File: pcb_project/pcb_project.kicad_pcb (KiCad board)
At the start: 8 copper layers, 234 parts, among them IC1 TPS54325PWPR, IC2 TPS54294PWPR, IC3 IS61WV204816BLL-10TLI, J1 Conn_01x10_Pin, J2 FTSH-107-01-F-DV-K, J3 Conn_ST_STDC14, J4 DE15_Socket_HighDensity_Mount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, J5 USB_B_Micro, J6 MEM2052-00-195-00-A, J7 USB_A, Q1 BC857BS, Q2 BC847BPN, U1 XC7A100T-FTG256, U2 STM32U595VJTx, U3 TPS2041B, U4 D3V3XA4B10LP, U7 MAX7221xWG, U8 COM-11405, U9 MT25QL128ABA1ESE-0SIT, Y1 48MHz, Y2 XLH736025.175000I

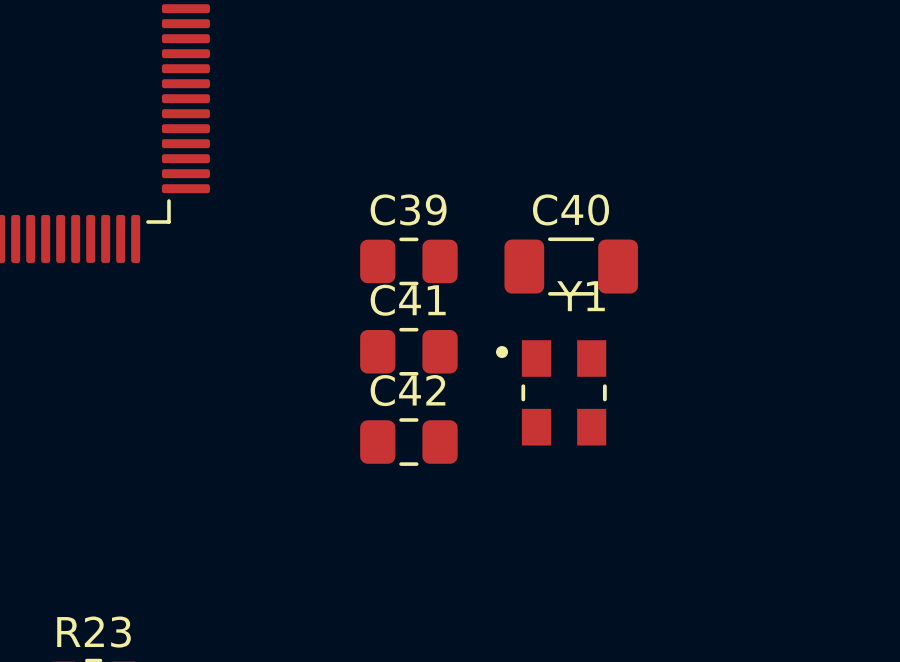
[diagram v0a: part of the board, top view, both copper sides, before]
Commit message: Add debounce cap on FPGA reset, add second sram symbol
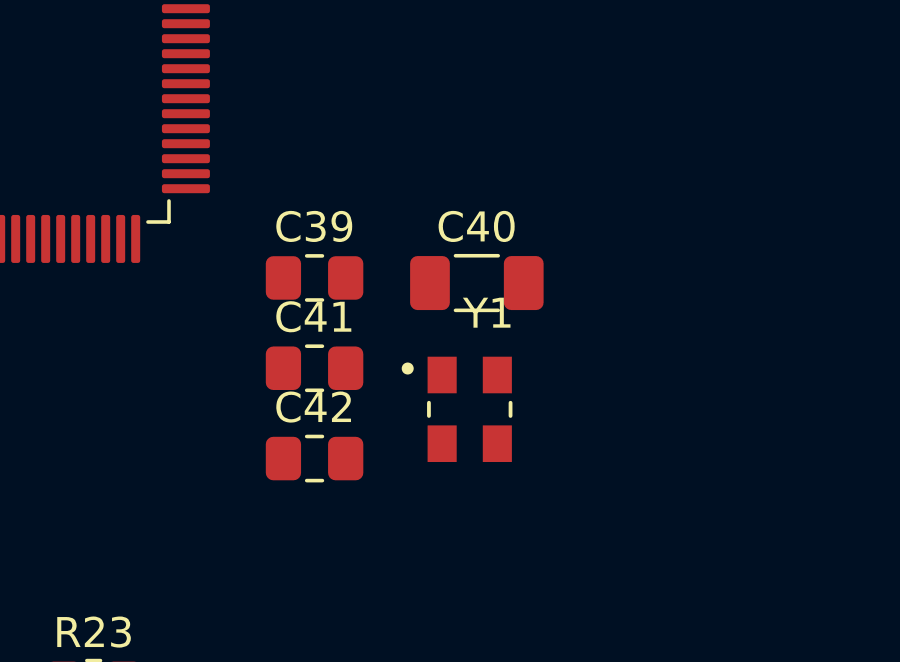
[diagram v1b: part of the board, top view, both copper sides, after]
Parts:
- moved C41 3.19 mm to (205.0, 124.5)
- moved C39 3.19 mm to (205.0, 121.5)
- moved C40 3.19 mm to (210.4, 121.7)
- moved C42 3.19 mm to (205.0, 127.5)
- moved Y1 3.19 mm to (210.1, 125.9)
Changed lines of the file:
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@@
 	(footprint "Capacitor_SMD:C_0805_2012Metric_Pad1.18x1.45mm_HandSolder"
 		(layer "F.Cu")
-		(at 208.107 126.97)
+		(at 204.9625 127.52)
 		(descr "Capacitor SMD 0805 (2012 Metric), square (rectangular) end terminal, IPC-7351 nominal with elongated pad for handsoldering. (Body size source: IPC-SM-782 page 76, https://www.pcb-3d.com/wordpress/wp-content/uploads/ipc-sm-782a_amendment_1_and_2.pdf, https://docs.google.com/spreadsheets/d/1BsfQQcO9C6DZCsRaXUlFlo91Tg2WpOkGARC1WS5S8t0/edit?usp=sharing), generated with kicad-footprint-generator")
 		(tags "capacitor handsolder")
@@
 	(footprint "Project_Footprints:OSCCC320X250X60N"
 		(layer "F.Cu")
-		(at 213.28 125.33)
+		(at 210.1355 125.88)
 		(property "Reference" "Y1"
 			(at 0.62907 -3.18457 0)
@@
 	(footprint "Capacitor_SMD:C_0805_2012Metric_Pad1.18x1.45mm_HandSolder"
 		(layer "F.Cu")
-		(at 208.107 123.96)
+		(at 204.9625 124.51)
 		(descr "Capacitor SMD 0805 (2012 Metric), square (rectangular) end terminal, IPC-7351 nominal with elongated pad for handsoldering. (Body size source: IPC-SM-782 page 76, https://www.pcb-3d.com/wordpress/wp-content/uploads/ipc-sm-782a_amendment_1_and_2.pdf, https://docs.google.com/spreadsheets/d/1BsfQQcO9C6DZCsRaXUlFlo91Tg2WpOkGARC1WS5S8t0/edit?usp=sharing), generated with kicad-footprint-generator")
 		(tags "capacitor handsolder")
@@
 	(footprint "Capacitor_SMD:C_1206_3216Metric_Pad1.33x1.80mm_HandSolder"
 		(layer "F.Cu")
-		(at 213.517 121.12)
+		(at 210.3725 121.67)
 		(descr "Capacitor SMD 1206 (3216 Metric), square (rectangular) end terminal, IPC-7351 nominal with elongated pad for handsoldering. (Body size source: IPC-SM-782 page 76, https://www.pcb-3d.com/wordpress/wp-content/uploads/ipc-sm-782a_amendment_1_and_2.pdf), generated with kicad-footprint-generator")
 		(tags "capacitor handsolder")
@@
 	(footprint "Capacitor_SMD:C_0805_2012Metric_Pad1.18x1.45mm_HandSolder"
 		(layer "F.Cu")
-		(at 208.107 120.95)
+		(at 204.9625 121.5)
 		(descr "Capacitor SMD 0805 (2012 Metric), square (rectangular) end terminal, IPC-7351 nominal with elongated pad for handsoldering. (Body size source: IPC-SM-782 page 76, https://www.pcb-3d.com/wordpress/wp-content/uploads/ipc-sm-782a_amendment_1_and_2.pdf, https://docs.google.com/spreadsheets/d/1BsfQQcO9C6DZCsRaXUlFlo91Tg2WpOkGARC1WS5S8t0/edit?usp=sharing), generated with kicad-footprint-generator")
 		(tags "capacitor handsolder")

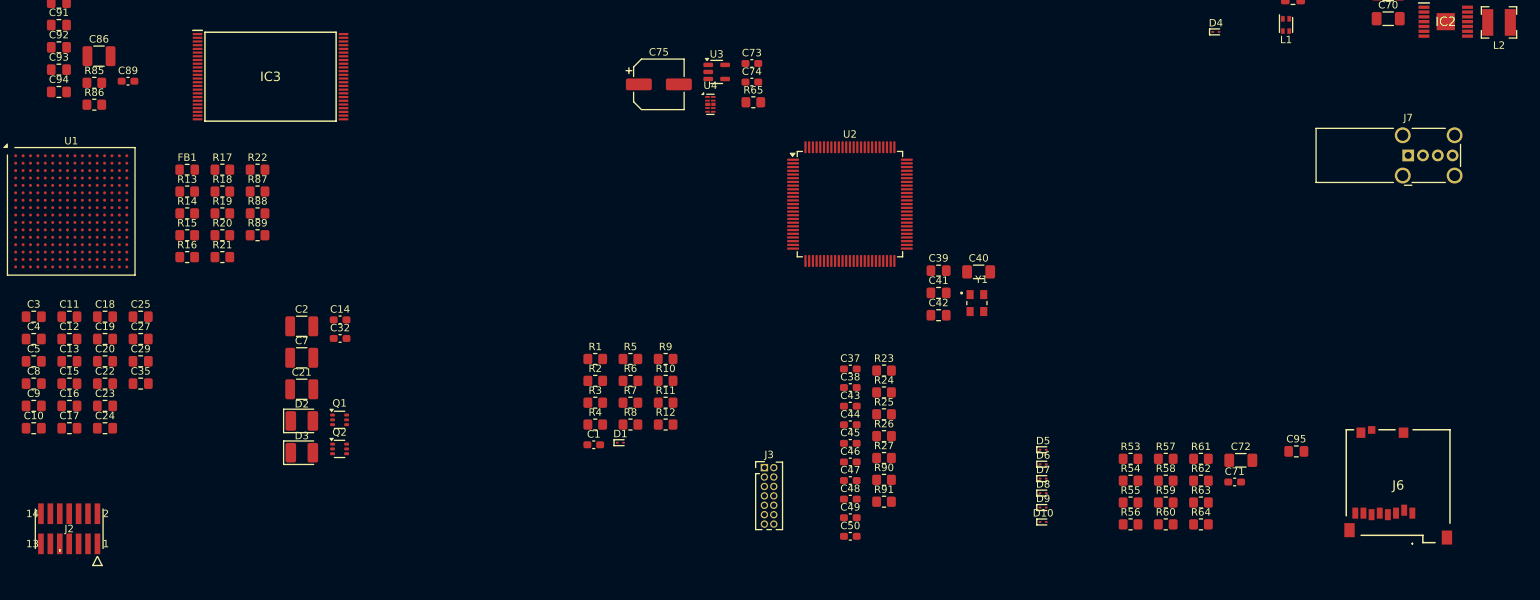
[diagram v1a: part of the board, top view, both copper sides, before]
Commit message: Initial MicroSD reader layout
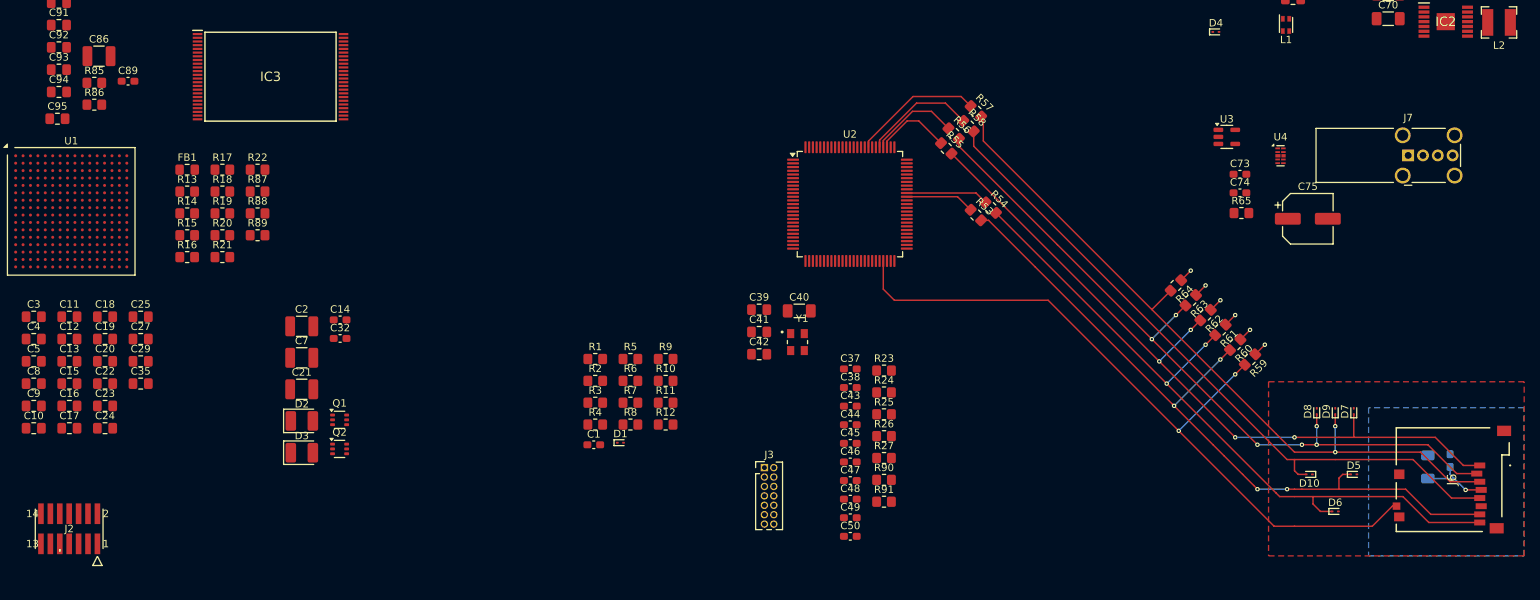
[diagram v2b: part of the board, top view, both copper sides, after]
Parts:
- C71, C72: moved to B.Cu
- moved C95 173.1 mm to (86.0, 101.0)
- moved C75 89.4 mm to (254.8, 114.5)
- moved U4 77.3 mm to (251.1, 106.0)
- moved U3 69.4 mm to (243.9, 103.5)
- moved C73 67.6 mm to (245.6, 108.5)
- moved C74 67.6 mm to (245.6, 111.0)
- moved R65 67.6 mm to (245.8, 113.7)
- moved R56 57.9 mm to (207.0, 103.0), turned to -45 degrees
- moved R58 54.8 mm to (209.0, 102.0), turned to -45 degrees
- moved R55 53.9 mm to (206.0, 105.0), turned to -45 degrees
- moved R57 53.4 mm to (210.0, 100.0), turned to -45 degrees
- moved D7 42.9 mm to (261.0, 140.5), turned to 90 degrees
- moved D5 42.1 mm to (261.0, 149.0)
- moved D9 41.5 mm to (258.5, 140.5), turned to 90 degrees
- moved R54 41.4 mm to (212.0, 113.0), turned to -45 degrees
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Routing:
- net /MCU/PB10_LPGPIO1_P4: track 0.00 -> 100.1 mm, vias 0 -> 2
- net Net-(D8-A1): track 0.00 -> 99.7 mm, vias 0 -> 6
- net Net-(D7-A1): track 0.00 -> 99.6 mm, vias 0 -> 4
- net Net-(D9-A1): track 0.00 -> 98.1 mm, vias 0 -> 2
- net Net-(D5-A1): track 0.00 -> 97.7 mm, vias 0 -> 4
- net Net-(D6-A1): track 0.00 -> 96.5 mm, vias 0 -> 2
- net Net-(D10-A2): track 0.00 -> 93.3 mm
- net +3V3: track 0.00 -> 20.6 mm, vias 0 -> 7
- net /MCU/PD2_SDMMC1_CMD: track 0.00 -> 17.7 mm
- net /MCU/PC12_SDMMC1_CK: track 0.00 -> 15.3 mm
- net /MCU/PC11_SDMMC1_D3: track 0.00 -> 12.3 mm
- net /MCU/PC9_SDMMC1_D1: track 0.00 -> 11.1 mm
- net /MCU/PC10_SDMMC1_D2: track 0.00 -> 10.5 mm
- net /MCU/PC8_SDMMC1_D0: track 0.00 -> 9.35 mm
- added copper zone on B.Cu, net GND
- added copper zone on F.Cu, net GND

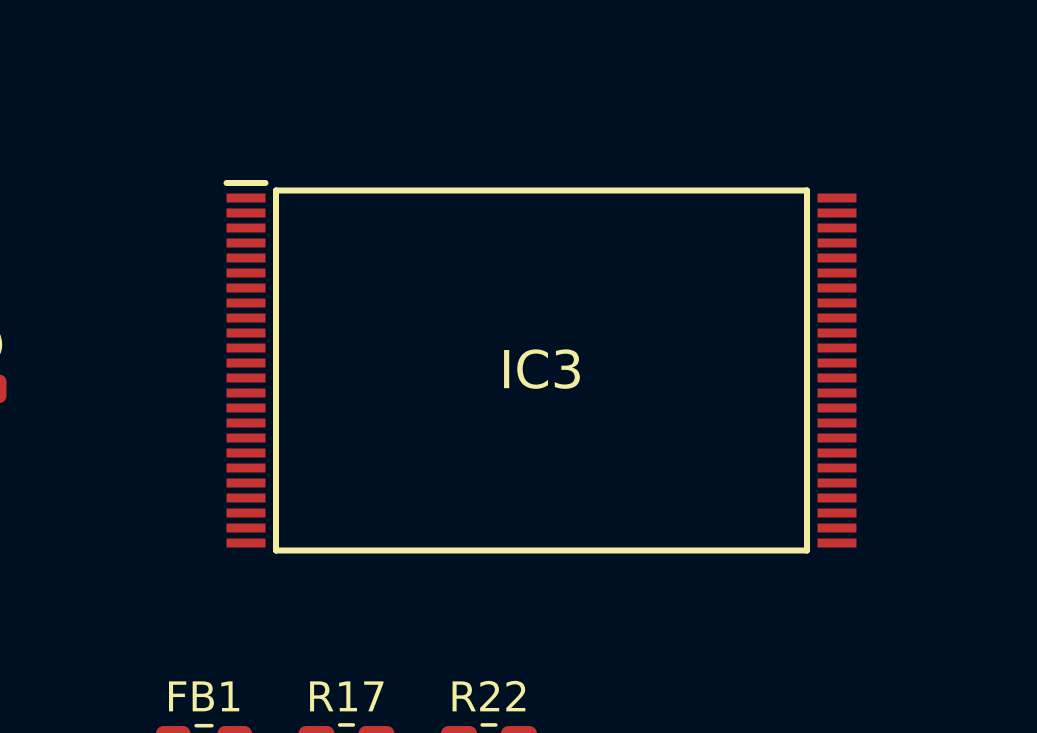
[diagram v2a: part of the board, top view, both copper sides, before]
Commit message: Add another SRAM
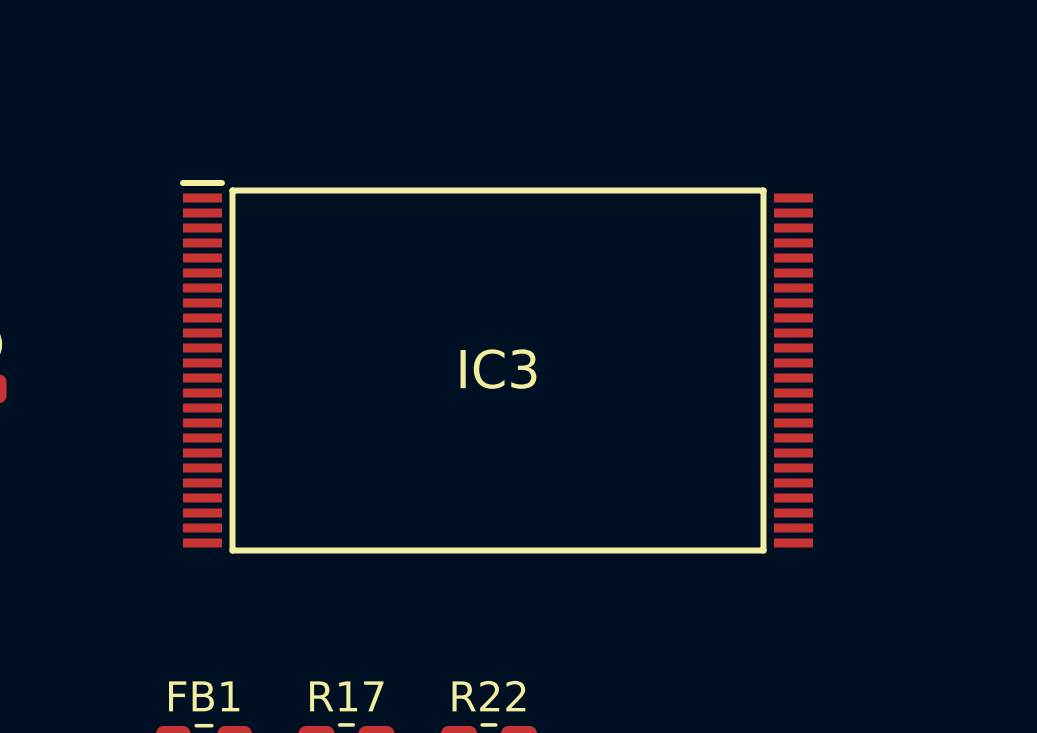
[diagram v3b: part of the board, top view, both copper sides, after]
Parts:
- moved IC3 1.45 mm to (113.3, 95.3)
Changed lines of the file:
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@@
 	(footprint "Project_Footprints:SOP50P2000X120-48N"
 		(layer "F.Cu")
-		(at 114.8 95.325)
+		(at 113.35 95.325)
 		(descr "TSOP 48")
 		(tags "Integrated Circuit")

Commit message: Fix ERC errors and update PCB from schematic
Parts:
- removed C79: 10nF, Capacitor_SMD:C_0603_1608Metric_Pad1.08x0.95mm_HandSolder
- removed C84: 1µF, Capacitor_SMD:C_0805_2012Metric_Pad1.18x1.45mm_HandSolder
- removed C96: 47µF, Capacitor_SMD:C_1210_3225Metric_Pad1.33x2.70mm_HandSolder
- removed JP1, JP2, JP3, JP4, JP5: Jumper_2_Bridged, Jumper:Jumper_Harwin_S1621_P10.9mm
- removed R72, R73, R87, R88, R89: 10k, Resistor_SMD:R_0805_2012Metric_Pad1.20x1.40mm_HandSolder
- removed R79: 22k, Resistor_SMD:R_0805_2012Metric_Pad1.20x1.40mm_HandSolder
- added C103(2-3mmfromvdd)2: 0.1µF, Capacitor_SMD:C_0603_1608Metric_Pad1.08x0.95mm_HandSolder, F.Cu at (139.5, 50.0)
- added C104: 10µF, Capacitor_SMD:C_1206_3216Metric_Pad1.33x1.80mm_HandSolder, F.Cu at (144.7, 50.4)
- added C105: 1µF, Capacitor_SMD:C_0805_2012Metric_Pad1.18x1.45mm_HandSolder, F.Cu at (144.1, 53.6)
- added C106(2-3mmfromvdd)2: 0.1µF, Capacitor_SMD:C_0603_1608Metric_Pad1.08x0.95mm_HandSolder, F.Cu at (139.5, 52.5)
- added C79 (2-3mm from SRAM Vdd)1: 0.1µF, Capacitor_SMD:C_0603_1608Metric_Pad1.08x0.95mm_HandSolder, F.Cu at (139.5, 55.0)
- added D11: PESD3V3U1UL, Diode_SMD:D_SOD-882, F.Cu at (160.8, 70.9)
- added D12: PESD3V3U1UL, Diode_SMD:D_SOD-882, F.Cu at (167.6, 43.9)
- added IC4: IS61WV204816BLL-10TLI, Project_Footprints:SOP50P2000X120-48N, F.Cu at (138.8, 116.8)
- added J10: M20-9990246, Project_Footprints:HARWIN_M20-9990246, F.Cu at (136.4, 68.5)
- added J11: M20-9990246, Project_Footprints:HARWIN_M20-9990246, F.Cu at (136.4, 72.6)
- added J12: M20-9990246, Project_Footprints:HARWIN_M20-9990246, F.Cu at (136.4, 76.7)
- added J8: M20-9990246, Project_Footprints:HARWIN_M20-9990246, F.Cu at (136.4, 60.3)
- added J9: M20-9990246, Project_Footprints:HARWIN_M20-9990246, F.Cu at (136.4, 64.4)
- added L3: 1.5u, Inductor_SMD:L_Bourns_SRP5030T, F.Cu at (143.7, 61.7)
- added L4: 2.2u, Inductor_SMD:L_Bourns-SRN4018, F.Cu at (142.7, 67.8)
- added SW2: SW_SPDT, Button_Switch_THT:SW_Slide_SPDT_Straight_CK_OS102011MS2Q, F.Cu at (153.7, 61.8)
- added SW3: SW_SPST, Button_Switch_THT:SW_TH_Tactile_Omron_B3F-100x, F.Cu at (151.3, 66.4)
- added SW4: SW_SPST, Button_Switch_THT:SW_TH_Tactile_Omron_B3F-100x, F.Cu at (163.5, 36.6)
- C76, C77, C78: value 10nF -> 100nF
- C85 (2-3mm from vdd)1: renamed from C85
- L2: footprint Inductor_SMD:L_Bourns-SRN4018 -> Inductor_SMD:L_Bourns_SRP5030T
- R66: value 10k -> 22k
- R67, R68, R69, R70, R71: value 10k -> 47K
- U9: footprint Project_Footprints:SOP2_8PIN_208MIL_MRN-LFPGA_FLASH -> Project_Footprints:SOP2_8PIN_208MIL_MRNFPGA_FLASH
- moved R67 181.4 mm to (134.9, 36.5), turned to 0 degrees
- moved R68 178.7 mm to (134.9, 39.4), turned to 0 degrees
- moved R69 176.1 mm to (134.9, 42.4), turned to 0 degrees
- moved R70 173.6 mm to (134.9, 45.3), turned to 0 degrees
- moved R71 171.1 mm to (134.9, 48.3), turned to 0 degrees
- moved R66 169.4 mm to (164.2, 48.8), turned to 0 degrees
- moved C78 169.1 mm to (164.0, 44.0), turned to 0 degrees
- moved C76 147.5 mm to (161.6, 66.0), turned to 0 degrees
- moved C77 144.7 mm to (161.6, 68.5), turned to 0 degrees
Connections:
- C76 pad 1: /Controller/V1 -> +3V3
- C77 pad 1: /Controller/V2 -> Net-(D11-K)
- C78 pad 1: /Controller/H1 -> /FPGA/FPGA_PROGRAM_B
- IC3 pad 12: +3.3V -> +3V3
- IC3 pad 36: +3.3V -> +3V3
- J3 pad 12: Net-(J3-~{RST}) -> Net-(D11-K)
- Q1 pad 1: +3.3V -> +3V3
- R15 pad 2: +3.3V -> +3V3
- R17 pad 2: +3.3V -> +3V3
- R18 pad 1: +3.3V -> +3V3
- R22 pad 1: +3.3V -> +3V3
- R66 pad 2: /Controller/B1 -> /FPGA/OSPI CS
- R67 pad 2: /Controller/B2 -> Net-(IC4-OE#)
- R68 pad 1: /Controller/V1 -> +3V3
- R68 pad 2: Net-(U5-V) -> Net-(IC4-LB#)
- R69 pad 1: /Controller/V2 -> +3V3
- R69 pad 2: Net-(U6-V) -> Net-(IC4-UB#)
- R70 pad 1: /Controller/H1 -> +3V3
- R70 pad 2: Net-(U5-H) -> Net-(IC4-CS#)
- R71 pad 1: /Controller/H2 -> +3V3
- R71 pad 2: Net-(U6-H) -> Net-(IC4-WE#)
- R77 pad 1: Net-(U1A-IO_L2P_T0_D02_14) -> +3V3
- R77 pad 2: +3V3 -> Net-(U1A-IO_L2P_T0_D02_14)
- R78 pad 1: Net-(U1A-IO_L6P_T0_FCS_B_14) -> +3V3
- R78 pad 2: +3V3 -> Net-(U1A-IO_L6P_T0_FCS_B_14)
- U1 pad A2: unconnected-(U1B-IO_L8N_T1_AD14N_35-PadA2) -> /FPGA/OSPI 3
- U1 pad B1: unconnected-(U1B-IO_L9N_T1_DQS_AD7N_35-PadB1) -> /FPGA/OSPI 0
- U1 pad B2: unconnected-(U1B-IO_L8P_T1_AD14P_35-PadB2) -> /FPGA/OSPI 4
- U1 pad C1: unconnected-(U1B-IO_L9P_T1_DQS_AD7P_35-PadC1) -> /FPGA/OSPI 1
- U1 pad C2: unconnected-(U1B-IO_L7N_T1_AD6N_35-PadC2) -> /FPGA/OSPI 5
- U1 pad C3: unconnected-(U1B-IO_L7P_T1_AD6P_35-PadC3) -> /FPGA/OSPI 7
- U1 pad C4: /VGA/R0 -> unconnected-(U1B-IO_L12N_T1_MRCC_35-PadC4)
- U1 pad D1: unconnected-(U1B-IO_L10N_T1_AD15N_35-PadD1) -> /FPGA/OSPI 2
- U1 pad E1: /VGA/G1 -> /VGA/R4
- U1 pad E2: unconnected-(U1B-IO_L10P_T1_AD15P_35-PadE2) -> /FPGA/OSPI 6
- U1 pad E5: /VGA/R2 -> /VGA/R0
- U1 pad E6: unconnected-(U1B-IO_0_35-PadE6) -> /FPGA/OSPI CS
- U1 pad F2: /VGA/G0 -> /VGA/R3
- U1 pad F3: /VGA/R4 -> /VGA/R2
- U1 pad F4: /VGA/R3 -> /VGA/R1
- U1 pad F5: /VGA/R1 -> /FPGA/OSPI CLK
- U1 pad G1: /VGA/G5 -> /VGA/G3
- U1 pad G2: /VGA/G4 -> /VGA/G2
- U1 pad G4: /VGA/G3 -> /VGA/G1
- U1 pad G5: /VGA/G2 -> /VGA/G0
- U1 pad H4: unconnected-(U1B-IO_L18N_T2_35-PadH4) -> /VGA/G5
- U1 pad H5: unconnected-(U1B-IO_L18P_T2_35-PadH5) -> /VGA/G4
- U1 pad K12: unconnected-(U1A-IO_0_14-PadK12) -> Net-(IC4-I/O15)
- U1 pad K13: unconnected-(U1A-IO_L5P_T0_D06_14-PadK13) -> Net-(IC4-I/O0)
- U1 pad L13: unconnected-(U1A-IO_L5N_T0_D07_14-PadL13) -> Net-(IC4-I/O1)
- U1 pad L14: unconnected-(U1A-IO_L4P_T0_D04_14-PadL14) -> Net-(IC4-I/O14)
- U1 pad M12: unconnected-(U1A-IO_L6N_T0_D08_VREF_14-PadM12) -> Net-(IC4-WE#)
- U1 pad M14: unconnected-(U1A-IO_L4N_T0_D05_14-PadM14) -> Net-(IC4-I/O13)
- U1 pad M16: unconnected-(U1A-IO_L7P_T1_D09_14-PadM16) -> Net-(IC4-I/O2)
- U1 pad M6: unconnected-(U1A-IO_L19P_T3_A10_D26_14-PadM6) -> Net-(IC4-A8)
- U1 pad M9: +3.3V -> +3V3
- U1 pad N11: unconnected-(U1A-IO_L13P_T2_MRCC_14-PadN11) -> Net-(IC4-LB#)
- U1 pad N12: unconnected-(U1A-IO_L13N_T2_MRCC_14-PadN12) -> Net-(IC4-UB#)
- U1 pad N14: /FPGA/OSPI CLK -> Net-(IC4-A14)
- U1 pad N16: unconnected-(U1A-IO_L7N_T1_D10_14-PadN16) -> Net-(IC4-I/O12)
- U1 pad N6: unconnected-(U1A-IO_L19N_T3_A09_D25_VREF_14-PadN6) -> Net-(IC4-A7)
- U1 pad N9: unconnected-(U1A-IO_L18P_T2_A12_D28_14-PadN9) -> Net-(IC4-A12)
- U1 pad P10: unconnected-(U1A-IO_L14P_T2_SRCC_14-PadP10) -> Net-(IC4-A20)
- U1 pad P11: unconnected-(U1A-IO_L14N_T2_SRCC_14-PadP11) -> Net-(IC4-CS#)
- U1 pad P13: unconnected-(U1A-IO_L11N_T1_SRCC_14-PadP13) -> Net-(IC4-I/O4)
- U1 pad P14: unconnected-(U1A-IO_L12N_T1_MRCC_14-PadP14) -> Net-(IC4-I/O6)
- U1 pad P15: unconnected-(U1A-IO_L8P_T1_D11_14-PadP15) -> Net-(IC4-I/O11)
- U1 pad P16: unconnected-(U1A-IO_L8N_T1_D12_14-PadP16) -> Net-(IC4-I/O10)
- U1 pad P6: /FPGA/OSPI CS -> Net-(IC4-A6)
- U1 pad P8: unconnected-(U1A-IO_L20P_T3_A08_D24_14-PadP8) -> Net-(IC4-A10)
- U1 pad P9: unconnected-(U1A-IO_L18N_T2_A11_D27_14-PadP9) -> Net-(IC4-A13)
- U1 pad R10: /FPGA/OSPI 6 -> Net-(IC4-A16)
- U1 pad R11: /FPGA/OSPI 7 -> Net-(IC4-A17)
- U1 pad R12: unconnected-(U1A-IO_L15P_T2_DQS_RDWR_B_14-PadR12) -> Net-(IC4-OE#)
- U1 pad R13: unconnected-(U1A-IO_L16P_T2_CSI_B_14-PadR13) -> Net-(IC4-I/O5)
- U1 pad R15: unconnected-(U1A-IO_L9P_T1_DQS_14-PadR15) -> Net-(IC4-I/O9)
- U1 pad R16: unconnected-(U1A-IO_L9N_T1_DQS_D13_14-PadR16) -> Net-(IC4-I/O8)
- U1 pad R5: /FPGA/OSPI 2 -> Net-(IC4-A4)
- U1 pad R6: /FPGA/OSPI 3 -> Net-(IC4-A2)
- U1 pad R7: /FPGA/OSPI 4 -> Net-(IC4-A0)
- U1 pad R8: /FPGA/OSPI 5 -> Net-(IC4-A11)
- U1 pad T10: /FPGA/OSPI 1 -> Net-(IC4-A9)
- U1 pad T12: unconnected-(U1A-IO_L15N_T2_DQS_DOUT_CSO_B_14-PadT12) -> Net-(IC4-A18)
- U1 pad T13: unconnected-(U1A-IO_L16N_T2_A15_D31_14-PadT13) -> Net-(IC4-A19)
- U1 pad T14: unconnected-(U1A-IO_L10P_T1_D14_14-PadT14) -> Net-(IC4-I/O7)
- U1 pad T15: unconnected-(U1A-IO_L10N_T1_D15_14-PadT15) -> Net-(IC4-I/O3)
- U1 pad T5: unconnected-(U1A-IO_L23N_T3_A02_D18_14-PadT5) -> Net-(IC4-A5)
- U1 pad T7: unconnected-(U1A-IO_L21P_T3_DQS_14-PadT7) -> Net-(IC4-A1)
- U1 pad T8: unconnected-(U1A-IO_L21N_T3_DQS_A06_D22_14-PadT8) -> Net-(IC4-A3)
- U1 pad T9: /FPGA/OSPI 0 -> Net-(IC4-A15)
- U2 pad 14: Net-(J3-~{RST}) -> Net-(D11-K)

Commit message: Initial components positioning
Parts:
- C71, C72: moved to F.Cu
- moved J6 192.1 mm to (126.5, 27.0)
- moved D6 180.0 mm to (117.6, 42.0)
- moved D10 178.8 mm to (114.1, 39.0)
- moved D5 178.8 mm to (120.1, 39.0)
- moved D7 175.2 mm to (120.1, 36.5)
- moved D8 175.2 mm to (115.1, 36.5)
- moved D9 175.2 mm to (117.6, 36.5)
- moved C72 173.0 mm to (134.1, 42.2)
- moved C71 173.0 mm to (137.1, 41.4)
- moved R59 169.5 mm to (111.4, 31.7)
- moved R60 169.5 mm to (109.4, 29.7)
- moved R61 169.5 mm to (107.4, 27.7)
- moved R62 169.5 mm to (105.4, 25.7)
- moved R63 169.5 mm to (103.4, 23.7)
- moved R64 169.5 mm to (101.4, 21.7)
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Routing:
- net /MCU/PB10_LPGPIO1_P4: track 100.1 -> 0.00 mm, vias 2 -> 0
- net Net-(D8-A1): track 99.7 -> 0.00 mm, vias 6 -> 0
- net Net-(D7-A1): track 99.6 -> 0.00 mm, vias 4 -> 0
- net Net-(D9-A1): track 98.1 -> 0.41 mm, vias 2 -> 0
- net Net-(D5-A1): track 97.7 -> 0.00 mm, vias 4 -> 0
- net Net-(D6-A1): track 96.5 -> 0.00 mm, vias 2 -> 0
- net Net-(D10-A2): track 93.3 -> 0.00 mm
- net +3V3: track 20.6 -> 0.00 mm, vias 7 -> 0
- net /MCU/PD2_SDMMC1_CMD: track 17.7 -> 0.00 mm
- net /MCU/PC12_SDMMC1_CK: track 15.3 -> 0.00 mm
- net /MCU/PC11_SDMMC1_D3: track 12.3 -> 0.00 mm
- net /MCU/PC9_SDMMC1_D1: track 11.1 -> 0.00 mm
- net /MCU/PC10_SDMMC1_D2: track 10.5 -> 0.00 mm
- net /MCU/PC8_SDMMC1_D0: track 9.35 -> 0.00 mm
- removed copper zone on B.Cu, net GND
- removed copper zone on F.Cu, net GND
